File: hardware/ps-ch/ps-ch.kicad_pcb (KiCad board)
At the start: 2 copper layers, 230 parts, among them J1 Conn_02x16_Odd_Even, J2 Conn_02x16_Odd_Even, J3 Conn_01x05, K1 TX2SA-3V, Q1 BSS138, Q10 MMBT3906, Q11 MMBT3904, Q12 MMBT3904, Q2 BSS138, Q3 PSMN059-150Y, Q4 PSMN059-150Y, Q5 MMBT3904, Q6 BSS138, Q7 PSMN059-150Y, Q8 PSMN059-150Y, Q9 MMBT3906, T1 750311590, U1 LMR51610X, U10 STM32C031K4Tx, U11 AD5686RBRUZ, U12 ADS1118IDGS, U13 LM74502H, U14 74LVC126A, U15 OPA992IDBVR, U16 OPA992IDBVR, U17 OPA992IDBVR, U18 INA301A3, U2 LM61495, U3 ADuM1401xRW, U4 ADuM1401xRW, U5 OPA992IDBVR, U6 LT8306, U7 LT8309, U8 OPA992IDBVR, U9 OPA992IDBVR

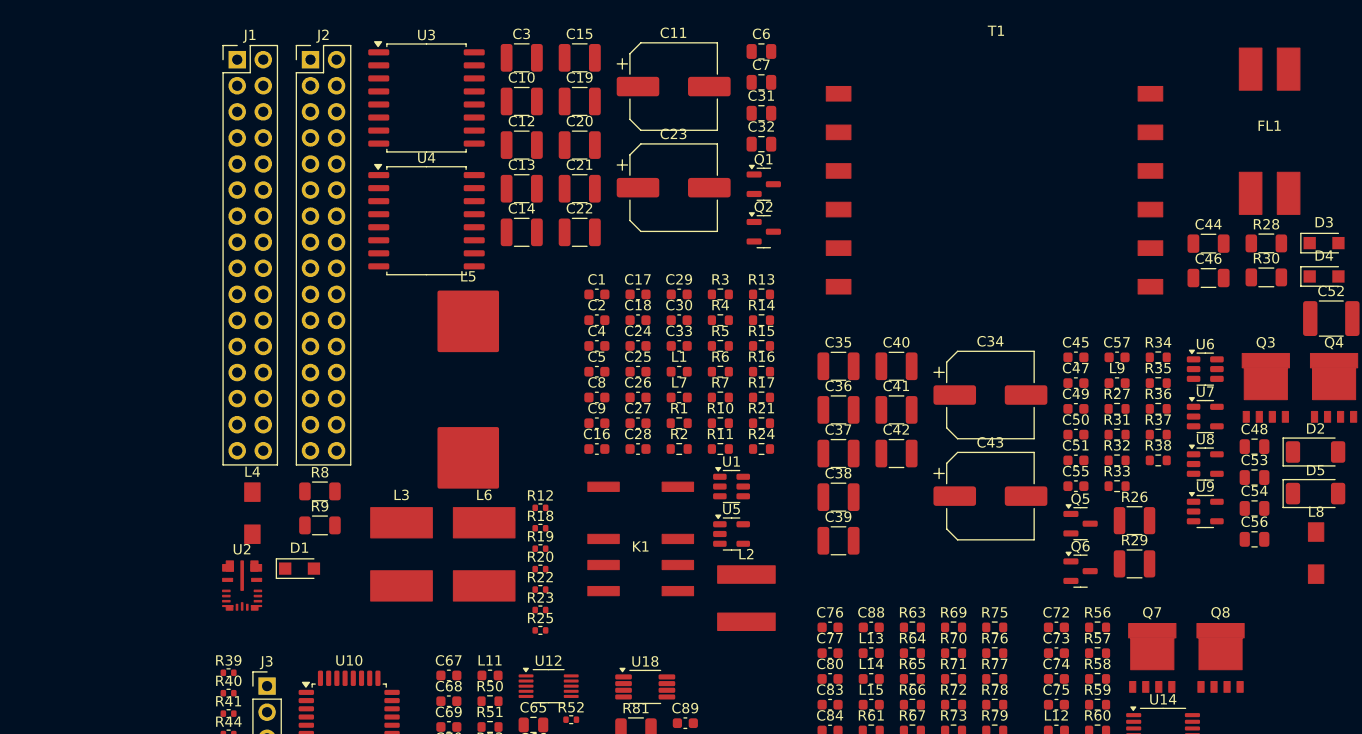
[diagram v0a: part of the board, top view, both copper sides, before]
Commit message: removed cmc, replaced input/output connectors
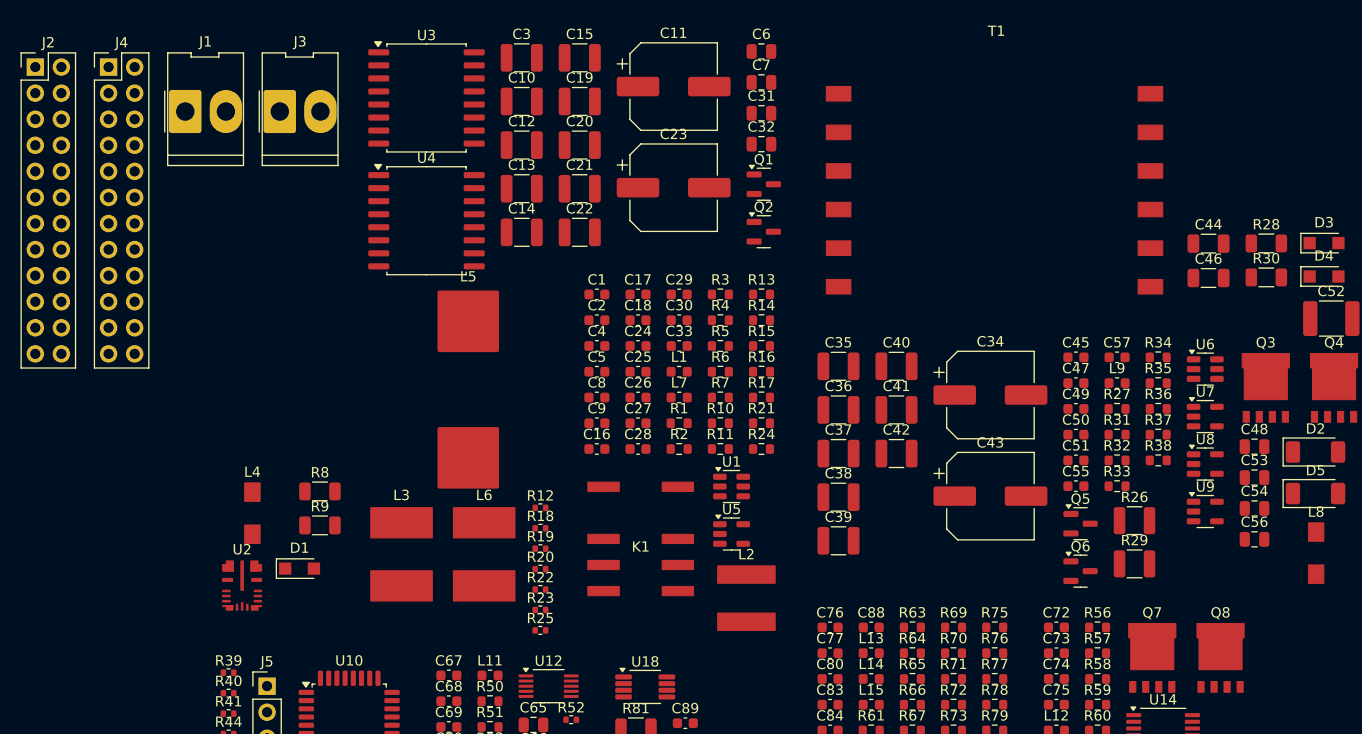
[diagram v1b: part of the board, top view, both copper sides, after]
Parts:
- removed FL1: MSD1583-123ME_, ps-ch:MSD1583
- added J3: 09652028, ps-ch:09652028, F.Cu at (88.5, 49.4)
- added J4: Conn_02x12_Odd_Even, Connector_PinHeader_2.54mm:PinHeader_2x12_P2.54mm_Vertical, F.Cu at (71.8, 45.1)
- J1: value Conn_02x16_Odd_Even -> 09652028; footprint Connector_PinHeader_2.54mm:PinHeader_2x16_P2.54mm_Vertical -> ps-ch:09652028
- J2: value Conn_02x16_Odd_Even -> Conn_02x12_Odd_Even; footprint Connector_PinHeader_2.54mm:PinHeader_2x16_P2.54mm_Vertical -> Connector_PinHeader_2.54mm:PinHeader_2x12_P2.54mm_Vertical
- moved J2 26.8 mm to (64.7, 45.1)
- moved J1 7.15 mm to (79.3, 49.4)
- renumbered J3 to J5
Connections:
- C25 pad 1: PRI_LO -> Earth
- C29 pad 1: PRI_LO -> Earth
- C34 pad 1: Net-(C34-Pad1) -> PRI_HI
- C53 pad 2: Net-(C34-Pad1) -> PRI_HI
- J1 pad 2: PRI_LO -> Earth
- J2 pad 1: PRI_HI -> 3V3
- J2 pad 10: PRI_LO -> Earth
- J2 pad 11: PRI_LO -> Earth
- J2 pad 12: 3V3 -> UART0_RX
- J2 pad 13: ACTIVATE_BOOTLOADER -> UART1_TX
- J2 pad 14: PRI_LO -> Earth
- J2 pad 15: PRI_LO -> Earth
- J2 pad 16: NRST -> UART1_RX
- J2 pad 17: UART1_TX -> UART2_TX
- J2 pad 18: PRI_LO -> Earth
- J2 pad 19: PRI_LO -> Earth
- J2 pad 2: PRI_LO -> Earth
- J2 pad 20: UART1_RX -> UART2_RX
- J2 pad 21: UART2_TX -> UART3_TX
- J2 pad 22: PRI_LO -> Earth
- J2 pad 23: PRI_LO -> Earth
- J2 pad 24: UART2_RX -> UART3_RX
- J2 pad 3: PRI_LO -> Earth
- J2 pad 4: PRI_HI -> 3V3
- J2 pad 5: PRI_HI -> ACTIVATE_BOOTLOADER
- J2 pad 6: PRI_LO -> Earth
- J2 pad 7: PRI_LO -> Earth
- J2 pad 8: PRI_HI -> NRST
- J2 pad 9: 3V3 -> UART0_TX
- L8 pad 2: Net-(C34-Pad1) -> PRI_HI
- L9 pad 2: Net-(C34-Pad1) -> PRI_HI
- R13 pad 1: PRI_LO -> Earth
- R24 pad 1: PRI_LO -> Earth
- U3 pad 15: PRI_LO -> Earth
- U3 pad 9: PRI_LO -> Earth
- U4 pad 2: PRI_LO -> Earth
- U4 pad 8: PRI_LO -> Earth

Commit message: started floorplanning
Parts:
- removed C85: 10μF 0805 50Vdc X5R ±20%, Capacitor_SMD:C_0805_2012Metric
- removed L14, L15: 60Ω@100MHz, Inductor_SMD:L_0603_1608Metric
- added H1: MountingHole_Pad, MountingHole:MountingHole_3.2mm_M3_Pad, F.Cu at (310.5, 44.5)
- added H2: MountingHole_Pad, MountingHole:MountingHole_3.2mm_M3_Pad, F.Cu at (254.0, 44.5)
- added H3: MountingHole_Pad, MountingHole:MountingHole_3.2mm_M3_Pad, F.Cu at (255.0, 174.5)
- added H4: MountingHole_Pad, MountingHole:MountingHole_3.2mm_M3_Pad, F.Cu at (309.0, 175.0)
- C81: value 10μF 0805 50Vdc X5R ±20% -> 0.1μF 0603 100Vdc X7R ±20%; footprint Capacitor_SMD:C_0805_2012Metric -> Capacitor_SMD:C_0603_1608Metric
- moved D1 258.8 mm to (340.0, 162.5), turned to 90 degrees
- moved J4 237.3 mm to (309.0, 54.0)
- moved C31 233.0 mm to (294.5, 219.8)
- moved C32 233.0 mm to (294.5, 222.8)
- moved C33 233.0 mm to (286.5, 242.5)
- moved L7 233.0 mm to (286.5, 247.5)
- moved Q2 225.5 mm to (332.5, 171.0)
- moved C28 221.2 mm to (326.0, 171.0)
- moved C81 220.5 mm to (353.5, 199.0)
- moved K1 216.1 mm to (328.0, 162.5), turned to 90 degrees
- moved C9 212.4 mm to (269.4, 230.2)
- moved R11 212.4 mm to (281.4, 232.7)
- moved R14 212.4 mm to (285.4, 220.2)
- moved R15 212.4 mm to (285.4, 222.7)
- moved R16 212.4 mm to (285.4, 225.2)
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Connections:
- net /ADC/SCLK renamed /SCK
- net /ADC/SDIN renamed /MOSI
- net /ADC/SDOUT renamed /MISO
- net /ADC/~{SYNC} renamed /~{ADC_CS}
- net /Current Measurement/~{ALERT} renamed /~{OCP}
- net /DAC/~{SYNC} renamed /~{DAC_CS}
- net /STM32/DISCHARGE_OUTPUT renamed /DISCHARGE
- net /STM32/ENABLE_OUTPUT renamed /EN_OUTPUT
- net /STM32/ENABLE_PWR_SPL renamed /EN_PWR_SPL
- C81 pad 2: VDC -> +3V3
- C82 pad 2: Net-(U16B-V+) -> Net-(U15B-V+)
- C83 pad 2: Net-(U16B-V+) -> Net-(U15B-V+)
- C86 pad 2: Net-(U17B-V+) -> Net-(U15B-V+)
- C87 pad 2: Net-(U17B-V+) -> Net-(U15B-V+)
- U16 pad 5: Net-(U16B-V+) -> Net-(U15B-V+)
- U17 pad 5: Net-(U17B-V+) -> Net-(U15B-V+)
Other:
- board outline added: 65 x 130 mm
